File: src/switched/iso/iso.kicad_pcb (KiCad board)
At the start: 2 copper layers, 100 x 45 mm, 66 parts, among them IC1 NCP1252ADR2G, J1 Conn_01x02, J2 Conn_01x02, J3 Conn_01x02, J4 Conn_01x02, Q1 TSD5N50MR, Q2 TSD5N50MR, T1 Transformer_1P_1S, U1 NCP5106, U2 ORPC-817C, U3 TL431LP, U4 MC34072, U5 LM317_SOT-223

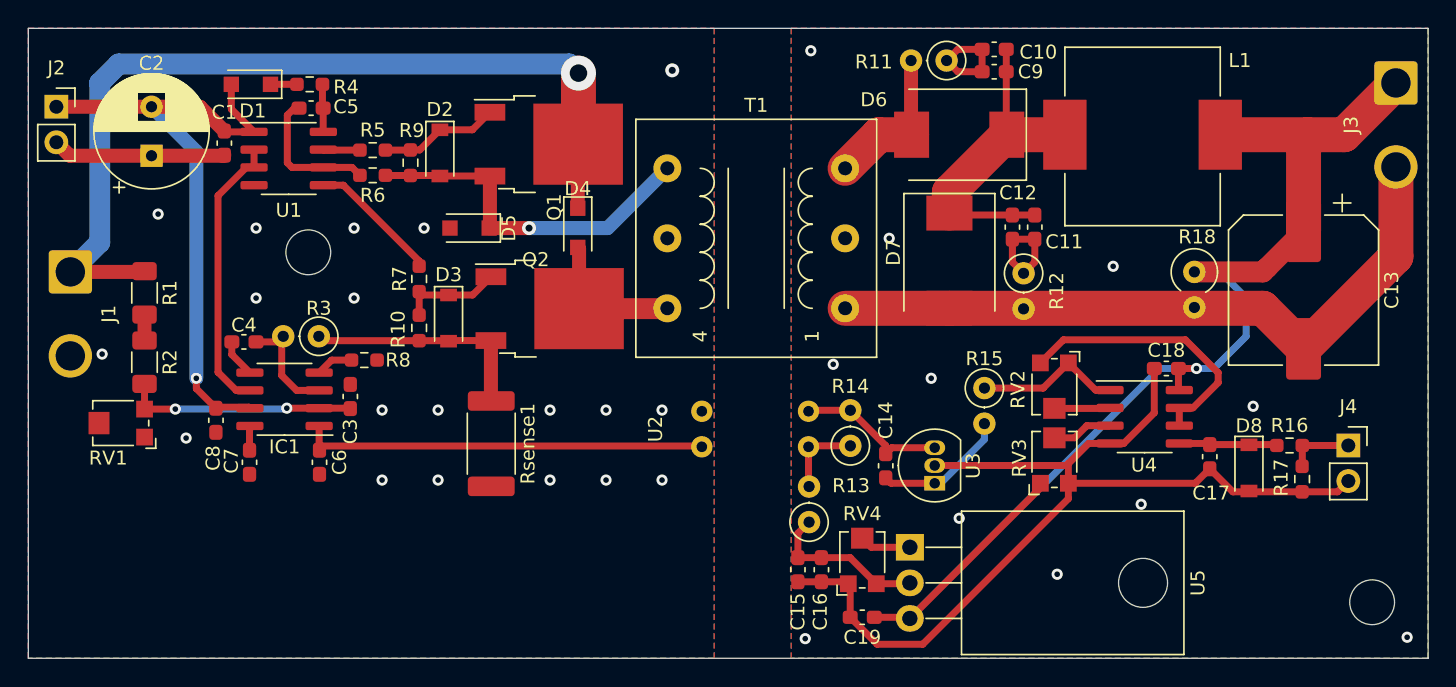
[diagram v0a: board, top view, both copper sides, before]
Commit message: Iso output changed to ceramic caps
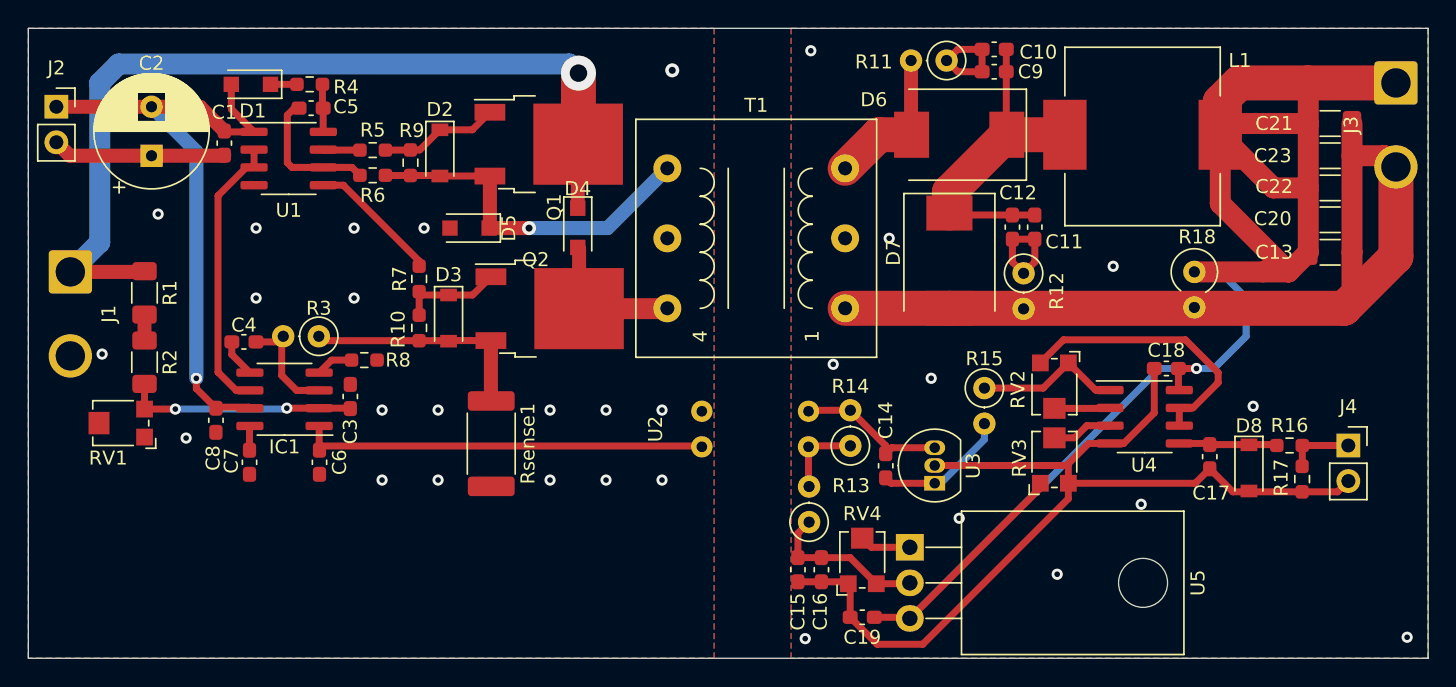
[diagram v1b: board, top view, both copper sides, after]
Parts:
- removed REF** (x2): MountingHole_3.2mm_M3, MountingHole:MountingHole_3.2mm_M3
- added C20: 10u, Capacitor_SMD:C_1206_3216Metric_Pad1.33x1.80mm_HandSolder, F.Cu at (269.0, 95.7)
- added C21: 10u, Capacitor_SMD:C_1206_3216Metric_Pad1.33x1.80mm_HandSolder, F.Cu at (269.0, 88.8)
- added C22: 10u, Capacitor_SMD:C_1206_3216Metric_Pad1.33x1.80mm_HandSolder, F.Cu at (269.0, 93.4)
- added C23: 10u, Capacitor_SMD:C_1206_3216Metric_Pad1.33x1.80mm_HandSolder, F.Cu at (269.0, 91.1)
- C13: value 330u -> 10u; footprint Capacitor_SMD:CP_Elec_10x14.3 -> Capacitor_SMD:C_1206_3216Metric_Pad1.33x1.80mm_HandSolder
- moved C13 3.30 mm to (269.0, 98.0), turned to 0 degrees
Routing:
- net /voutp: track 88.6 -> 121.1 mm
- net /voutn: track 120.9 -> 135.4 mm

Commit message: final boards and initial blinky
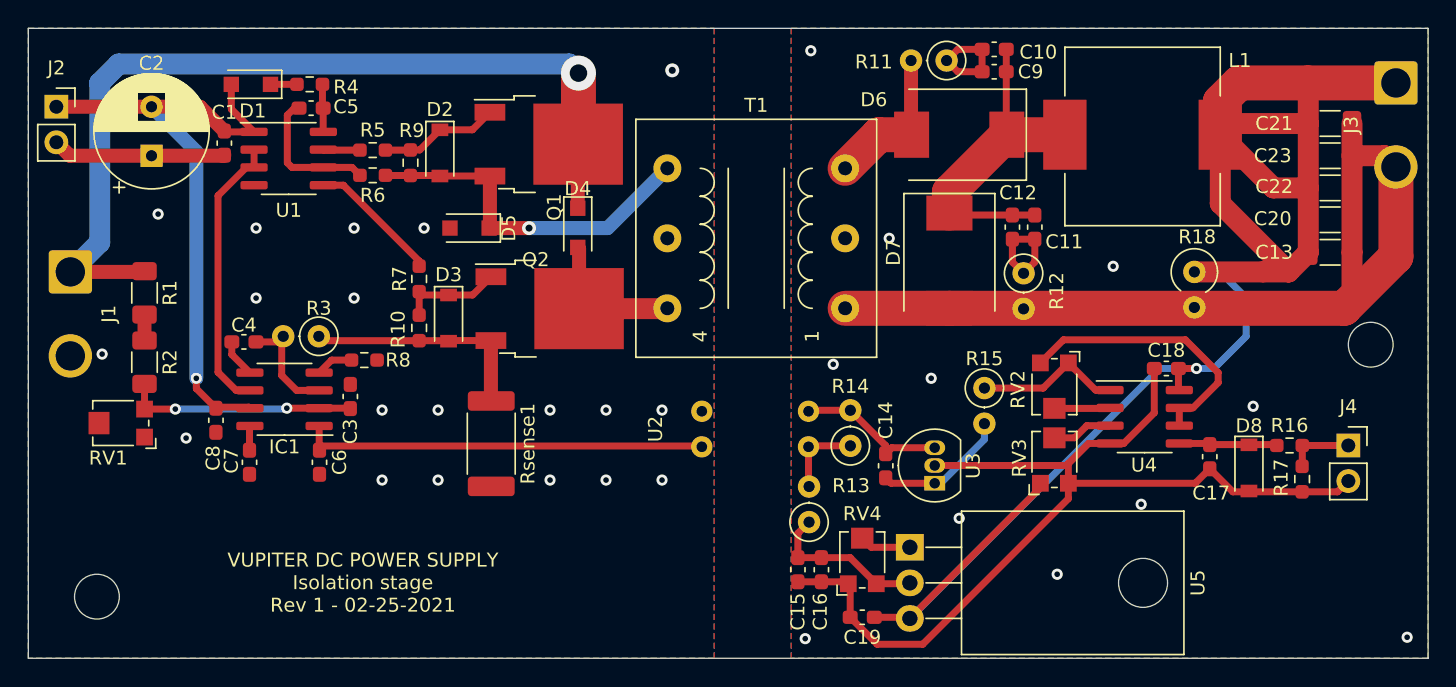
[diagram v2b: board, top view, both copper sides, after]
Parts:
- added REF**: MountingHole_3.2mm_M3, MountingHole:MountingHole_3.2mm_M3, F.Cu at (271.9, 104.6)
- added REF**: MountingHole_3.2mm_M3, MountingHole:MountingHole_3.2mm_M3, F.Cu at (180.9, 122.6)
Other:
- board text added: "VUPITER DC POWER SUPPLY Isolation stage Rev 1 - 02-25-2021"
